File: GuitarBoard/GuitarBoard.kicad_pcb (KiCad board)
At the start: 2 copper layers, 18 parts, among them J1 Pickups, J2 Input Jack, J3 Bridge Ground, J4 FXALeft, J5 FXARight, J6 FXBLeft, J7 FXBRight, J8 Output Jack, J9 Amp, SW1 Amp Knob Switch, SW2 Volume DPDT A, SW3 Volume DPDT B, SW4 Tone DPDT A, SW5 Tone DPDT B

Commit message: Added early version of add on board and reverse polarity protection to mainboard
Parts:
- added D1: D, Diode_THT:D_DO-41_SOD81_P10.16mm_Horizontal, F.Cu at (131.4, 39.4)
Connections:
- BT1 pad 1: 9V -> Net-(BT1-Pad1)

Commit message: Merging pedals into one board
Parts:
- removed J4: FXALeft, Connector_PinSocket_2.54mm:PinSocket_1x04_P2.54mm_Vertical
- removed J5: FXARight, Connector_PinSocket_2.54mm:PinSocket_1x04_P2.54mm_Vertical
- removed J6: FXBLeft, Connector_PinSocket_2.54mm:PinSocket_1x04_P2.54mm_Vertical
- removed J7: FXBRight, Connector_PinSocket_2.54mm:PinSocket_1x04_P2.54mm_Vertical
- added C10: 10uF, Capacitor_THT:CP_Axial_L10.0mm_D6.0mm_P15.00mm_Horizontal, F.Cu at (109.9, 102.6)
- added C11: 10uF, Capacitor_THT:CP_Axial_L10.0mm_D6.0mm_P15.00mm_Horizontal, F.Cu at (120.8, 81.4)
- added C2: 0.1uF, libraries:C_Flat_L7.2_H6.5, F.Cu at (175.8, 89.4)
- added C3: 0.1uF, libraries:C_Flat_L7.2_H6.5, F.Cu at (174.6, 79.6)
- added C4: 2200pF, libraries:C_Flat_L7.2_H6.5, F.Cu at (134.4, 112.5)
- added C5: 0.1uF, libraries:C_Flat_L7.2_H6.5, F.Cu at (147.7, 98.8)
- added C6: 4700pF, libraries:C_Flat_L7.2_H6.5, F.Cu at (158.3, 94.3)
- added C7: 0.1uF, libraries:C_Flat_L7.2_H6.5, F.Cu at (147.7, 108.6)
- added C8: 100pF, libraries:C_Flat_L7.2_H6.5, F.Cu at (167.0, 89.4)
- added C9: 1000pF, libraries:C_Flat_L7.2_H6.5, F.Cu at (156.4, 104.1)
- added D2: 1N4148, Diode_THT:D_DO-35_SOD27_P7.62mm_Horizontal, F.Cu at (154.8, 90.5)
- added D3: 1N4148, Diode_THT:D_DO-35_SOD27_P7.62mm_Horizontal, F.Cu at (147.2, 95.0)
- added D4: 1N4148, Diode_THT:D_DO-35_SOD27_P7.62mm_Horizontal, F.Cu at (163.5, 79.4)
- added IC1: CD4069UBE, SamacSys_Parts:DIP794W53P254L1930H508Q14N, F.Cu at (113.6, 88.2)
- added Q1: 2N3904, Package_TO_SOT_THT:TO-92_Inline, F.Cu at (164.0, 84.4)
- added Q2: 2N3904, Package_TO_SOT_THT:TO-92_Inline, F.Cu at (167.2, 100.5)
- added R1: 1M, Resistor_THT:R_Axial_DIN0207_L6.3mm_D2.5mm_P10.16mm_Horizontal, F.Cu at (133.9, 95.3)
- added R10: 10K, Resistor_THT:R_Axial_DIN0207_L6.3mm_D2.5mm_P10.16mm_Horizontal, F.Cu at (120.6, 87.2)
- added R11: 100K, Resistor_THT:R_Axial_DIN0207_L6.3mm_D2.5mm_P10.16mm_Horizontal, F.Cu at (109.7, 108.4)
- added R2: 1M, Resistor_THT:R_Axial_DIN0207_L6.3mm_D2.5mm_P10.16mm_Horizontal, F.Cu at (141.5, 91.2)
- added R3: 2M, Resistor_THT:R_Axial_DIN0207_L6.3mm_D2.5mm_P10.16mm_Horizontal, F.Cu at (120.6, 95.3)
- added R4: 4.7K, Resistor_THT:R_Axial_DIN0207_L6.3mm_D2.5mm_P10.16mm_Horizontal, F.Cu at (109.7, 116.5)
- added R5: 1M, Resistor_THT:R_Axial_DIN0207_L6.3mm_D2.5mm_P10.16mm_Horizontal, F.Cu at (123.0, 108.4)
- added R6: 47K, Resistor_THT:R_Axial_DIN0207_L6.3mm_D2.5mm_P10.16mm_Horizontal, F.Cu at (139.2, 79.6)
- added R7: 1M, Resistor_THT:R_Axial_DIN0207_L6.3mm_D2.5mm_P10.16mm_Horizontal, F.Cu at (109.7, 112.5)
- added R8: 10K, Resistor_THT:R_Axial_DIN0207_L6.3mm_D2.5mm_P10.16mm_Horizontal, F.Cu at (133.9, 87.2)
- added R9: 10K, Resistor_THT:R_Axial_DIN0207_L6.3mm_D2.5mm_P10.16mm_Horizontal, F.Cu at (128.2, 91.2)
- added RV3: 250K Distortion, Potentiometer_THT:Potentiometer_Bourns_3386F_Vertical, F.Cu at (124.3, 118.5)
- added RV4: 250K Volume, Potentiometer_THT:Potentiometer_Bourns_3386F_Vertical, F.Cu at (137.6, 105.4)
- added RV5: A10K, Potentiometer_THT:Potentiometer_Bourns_3386F_Vertical, F.Cu at (153.8, 85.7)

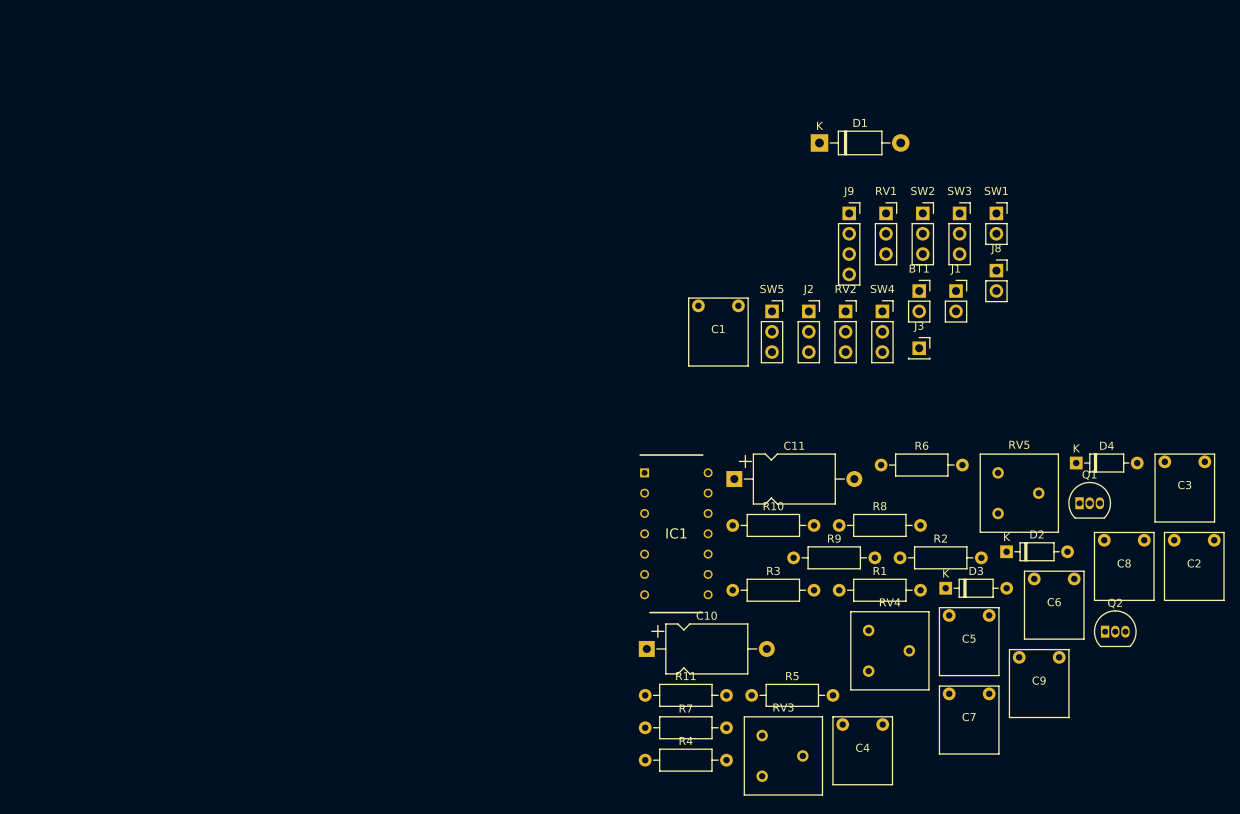
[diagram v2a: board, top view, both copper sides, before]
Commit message: Started tracing everything out
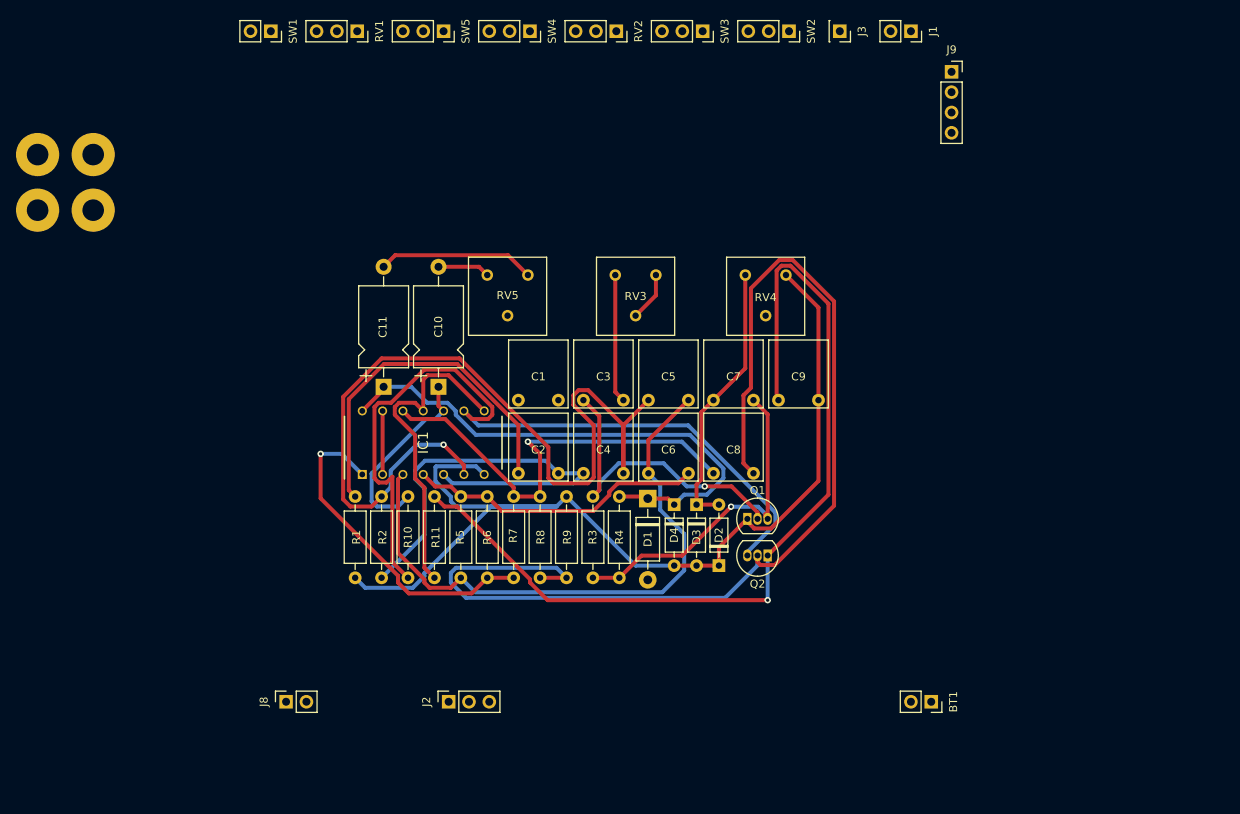
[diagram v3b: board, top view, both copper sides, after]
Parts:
- added H1: Mount, MountingHole:MountingHole_2.7mm_Pad, F.Cu at (33.7, 40.8)
- added H2: Mount, MountingHole:MountingHole_2.7mm_Pad, F.Cu at (33.7, 47.8)
- added H3: Mount, MountingHole:MountingHole_2.7mm_Pad, F.Cu at (40.7, 40.8)
- added H4: Mount, MountingHole:MountingHole_2.7mm_Pad, F.Cu at (40.7, 47.8)
- moved J8 103.9 mm to (64.8, 109.2), turned to 90 degrees
- moved SW1 93.5 mm to (62.9, 25.4), turned to 270 degrees
- moved C2 77.5 mm to (98.8, 80.3), turned to 180 degrees
- moved RV5 70.5 mm to (89.9, 55.9), turned to 270 degrees
- moved RV1 69.9 mm to (73.7, 25.4), turned to 270 degrees
- moved C3 68.2 mm to (106.9, 71.1), turned to 180 degrees
- moved J2 66.4 mm to (85.1, 109.2), turned to 90 degrees
- moved RV3 65.3 mm to (105.9, 55.9), turned to 270 degrees
- moved R2 64.9 mm to (76.7, 93.7), turned to 90 degrees
- moved R1 61.6 mm to (73.4, 83.6), turned to 270 degrees
- moved SW4 56.3 mm to (95.2, 25.4), turned to 270 degrees
- moved SW5 54.0 mm to (84.5, 25.4), turned to 270 degrees
- moved RV4 51.9 mm to (122.2, 55.9), turned to 270 degrees
- moved BT1 51.4 mm to (145.4, 109.2), turned to 270 degrees
- moved D4 50.5 mm to (113.3, 84.6), turned to 270 degrees
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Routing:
- net FXGND: track 0.00 -> 146.1 mm
- net Net-(C8-Pad1): track 0.00 -> 139.3 mm
- net /pin6: track 0.00 -> 113.5 mm, vias 0 -> 1
- net Net-(C9-Pad2): track 0.00 -> 112.5 mm, vias 0 -> 1
- net /pin9: track 0.00 -> 99.9 mm
- net /pin3: track 0.00 -> 75.5 mm
- net 9V: track 0.00 -> 67.1 mm
- net /pin5: track 0.00 -> 56.8 mm
- net /pin12: track 0.00 -> 54.6 mm, vias 0 -> 1
- net FXInB: track 0.00 -> 44.7 mm
- net Net-(C7-Pad1): track 0.00 -> 42.7 mm, vias 0 -> 1
- net /pin1: track 0.00 -> 42.2 mm, vias 0 -> 1
- net /pin11: track 0.00 -> 41.2 mm
- net Net-(C3-Pad2): track 0.00 -> 39.4 mm, vias 0 -> 1
- net /pin4: track 0.00 -> 37.2 mm
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
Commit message: Made new board. Still need to lay out all the traces
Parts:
- removed BT1: Battery, Connector_PinSocket_2.54mm:PinSocket_1x02_P2.54mm_Vertical
- removed J1: Pickups, Connector_PinSocket_2.54mm:PinSocket_1x02_P2.54mm_Vertical
- removed J2: Input Jack, Connector_PinSocket_2.54mm:PinSocket_1x03_P2.54mm_Vertical
- removed J3: Bridge Ground, Connector_PinSocket_2.54mm:PinSocket_1x01_P2.54mm_Vertical
- removed J8: Output Jack, Connector_PinSocket_2.54mm:PinSocket_1x02_P2.54mm_Vertical
- removed J9: Amp, Connector_PinSocket_2.54mm:PinSocket_1x04_P2.54mm_Vertical
- removed RV1: V 500K, Connector_PinSocket_2.54mm:PinSocket_1x03_P2.54mm_Vertical
- removed RV2: T 500K, Connector_PinSocket_2.54mm:PinSocket_1x03_P2.54mm_Vertical
- removed RV3: 250K Distortion, Potentiometer_THT:Potentiometer_Bourns_3386F_Vertical
- removed RV4: 250K Volume, Potentiometer_THT:Potentiometer_Bourns_3386F_Vertical
- removed RV5: A10K, Potentiometer_THT:Potentiometer_Bourns_3386F_Vertical
- removed SW2: Volume DPDT A, Connector_PinSocket_2.54mm:PinSocket_1x03_P2.54mm_Vertical
- removed SW3: Volume DPDT B, Connector_PinSocket_2.54mm:PinSocket_1x03_P2.54mm_Vertical
- removed SW4: Tone DPDT A, Connector_PinSocket_2.54mm:PinSocket_1x03_P2.54mm_Vertical
- removed SW5: Tone DPDT B, Connector_PinSocket_2.54mm:PinSocket_1x03_P2.54mm_Vertical
- added 8Bit In: 250K Input Volume, Potentiometer_THT:Potentiometer_Bourns_3386F_Vertical, F.Cu at (94.1, 84.0)
- added 8Bit Out: A10K, Potentiometer_THT:Potentiometer_Bourns_3386F_Vertical, F.Cu at (77.1, 84.0)
- added 9V: Battery, Connector_PinSocket_2.54mm:PinSocket_1x02_P2.54mm_Vertical, F.Cu at (152.0, 107.0)
- added A: Volume DPDT A, Connector_PinSocket_2.54mm:PinSocket_1x03_P2.54mm_Vertical, F.Cu at (141.6, 88.4)
- added A: Tone DPDT A, Connector_PinSocket_2.54mm:PinSocket_1x03_P2.54mm_Vertical, F.Cu at (105.1, 88.4)
- added Amp: Amp, Connector_PinSocket_2.54mm:PinSocket_1x04_P2.54mm_Vertical, F.Cu at (152.0, 94.0)
- added B: Volume DPDT B, Connector_PinSocket_2.54mm:PinSocket_1x03_P2.54mm_Vertical, F.Cu at (145.4, 88.4)
- added B: Tone DPDT B, Connector_PinSocket_2.54mm:PinSocket_1x03_P2.54mm_Vertical, F.Cu at (108.9, 88.4)
- added Bridge: Bridge Ground, Connector_PinSocket_2.54mm:PinSocket_1x01_P2.54mm_Vertical, F.Cu at (128.8, 79.0)
- added Dist Level: 250K Distortion, Potentiometer_THT:Potentiometer_Bourns_3386F_Vertical, F.Cu at (131.8, 84.0)
- added Dist Volume: 250K Volume, Potentiometer_THT:Potentiometer_Bourns_3386F_Vertical, F.Cu at (114.8, 84.0)
- added Input: Input Jack, Connector_PinSocket_2.54mm:PinSocket_1x03_P2.54mm_Vertical, F.Cu at (104.5, 115.0)
- added Output: Output Jack, Connector_PinSocket_2.54mm:PinSocket_1x02_P2.54mm_Vertical, F.Cu at (68.0, 115.0)
- added Pickup: Pickups, Connector_PinSocket_2.54mm:PinSocket_1x02_P2.54mm_Vertical, F.Cu at (121.7, 79.0)
- added Tone: T 500K, Connector_PinSocket_2.54mm:PinSocket_1x03_P2.54mm_Vertical, F.Cu at (104.5, 79.0)
- added Volume: V 500K, Connector_PinSocket_2.54mm:PinSocket_1x03_P2.54mm_Vertical, F.Cu at (146.1, 79.0)
- moved H4 130.1 mm to (152.0, 115.0)
- moved H2 122.6 mm to (152.0, 80.0)
- moved H3 77.2 mm to (62.0, 115.0)
- moved SW1 53.9 mm to (68.0, 79.0), turned to 90 degrees
- moved C10 50.3 mm to (125.9, 97.5)
- moved H1 48.3 mm to (62.0, 80.0)
- moved C7 44.9 mm to (141.7, 112.0), turned to 270 degrees
- moved C1 42.7 mm to (66.8, 99.3)
- moved R10 41.2 mm to (120.9, 98.6), turned to 270 degrees
- moved C3 41.1 mm to (136.9, 99.3)
- moved D1 41.1 mm to (147.8, 99.8)
- moved C9 40.9 mm to (132.3, 112.0), turned to 270 degrees
- moved D4 38.8 mm to (144.8, 107.2), turned to 90 degrees
- moved R11 36.8 mm to (113.3, 115.1), turned to 0 degrees
- moved IC1 35.6 mm to (107.0, 102.1), turned to 0 degrees
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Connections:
- net FXInB renamed Net-(C2-Pad2)
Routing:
- net Net-(C8-Pad1): track 139.3 -> 21.5 mm
- net Net-(C9-Pad2): track 112.5 -> 10.1 mm, vias 1 -> 0
- net /pin9: track 99.9 -> 13.5 mm
- net /pin6: track 113.5 -> 29.2 mm, vias 1 -> 0
- net /pin3: track 75.5 -> 2.66 mm
- net Net-(C7-Pad1): track 42.7 -> 113.7 mm, vias 1 -> 0
- net /pin12: track 54.6 -> 3.75 mm, vias 1 -> 0
- net 9V: track 67.1 -> 21.4 mm
- net /pin5: track 56.8 -> 11.9 mm
- net /pin1: track 42.2 -> 0.00 mm, vias 1 -> 0
- net Net-(C3-Pad2): track 39.4 -> 0.00 mm, vias 1 -> 0
- net Net-(J1-Pad1): track 0.00 -> 38.8 mm
- net FXOutA: track 0.00 -> 31.5 mm
- net Net-(C7-Pad2): track 34.0 -> 2.89 mm
- net /pin11: track 41.2 -> 15.3 mm
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- added copper zone on B.Cu, net GND
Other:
- board outline added: 100 x 45 mm
- board text added: "+"
- board text added: "9V"
- board text added: "GND"
- board text added: "Out"

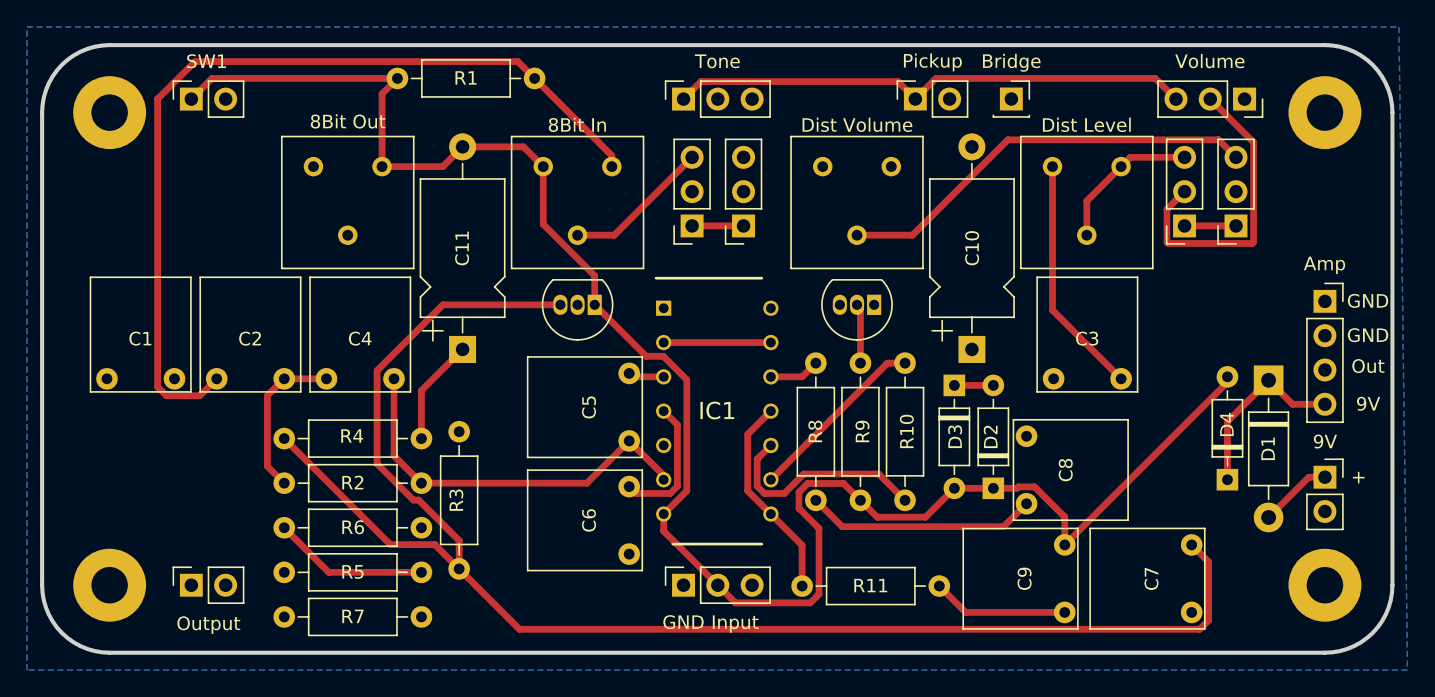
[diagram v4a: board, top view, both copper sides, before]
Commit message: Finalized GuitarBoard. Plotted and zipped Gerber files
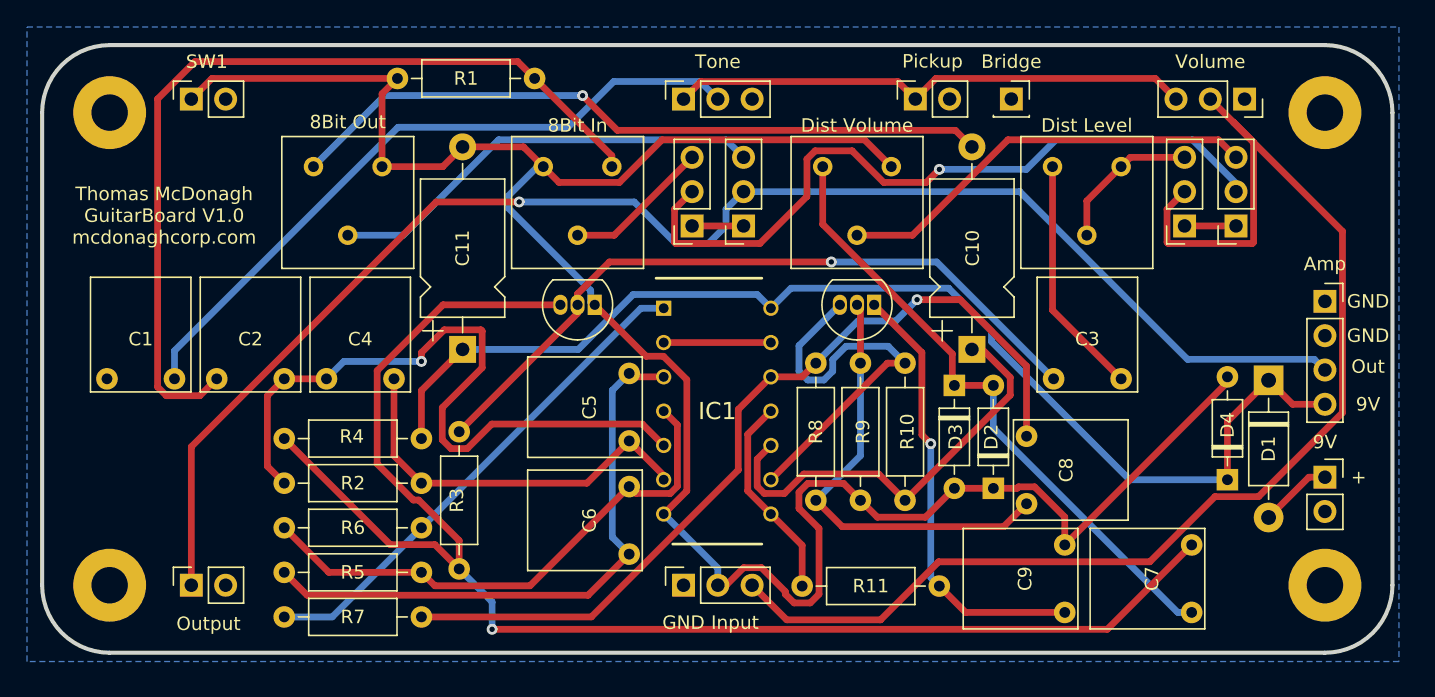
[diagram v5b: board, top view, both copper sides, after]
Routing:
- net Amp: track 0.00 -> 110.8 mm, vias 0 -> 1
- net Pickups: track 22.7 -> 98.7 mm
- net 9V: track 21.4 -> 87.1 mm
- net /pin12: track 3.75 -> 64.4 mm, vias 0 -> 1
- net Net-(SW3-Pad2): track 0.00 -> 54.6 mm, vias 0 -> 1
- net Net-(C3-Pad2): track 0.00 -> 53.7 mm, vias 0 -> 1
- net Net-(C10-Pad2): track 0.00 -> 52.5 mm, vias 0 -> 1
- net Net-(C1-Pad1): track 0.00 -> 51.1 mm
- net Net-(C7-Pad2): track 2.89 -> 46.6 mm
- net /pin3: track 2.66 -> 44.6 mm
- net /pin5: track 11.9 -> 52.7 mm, vias 0 -> 1
- net /pin1: track 0.00 -> 37.6 mm
- net FXOutB: track 0.00 -> 32.8 mm
- net FXGND: track 133.5 -> 165.6 mm
- net Net-(C9-Pad2): track 10.1 -> 32.9 mm, vias 0 -> 1
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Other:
- board text added: "Thomas McDonagh GuitarBoard V1.0 mcdonaghcorp.com"
